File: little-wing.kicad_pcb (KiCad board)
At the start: 2 copper layers, 116.8 x 96 mm, 72 parts, among them IC1 AP7335-WG-7, J1 nice!view, J2 Battery, J3 trackball, J4 trackball, SW1 Power, SW2 Reset, U1 nice!nano v2, U2 PMW3610

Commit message: Wiring up the MCU block
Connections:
- U1 pad 7: CS_T -> CS_D
- U1 pad 8: CS_D -> CS_T
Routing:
- net GND: track 590.5 -> 667.7 mm, vias 18 -> 19
- net Row 1: track 294.5 -> 367.0 mm, vias 17 -> 20
- net Col 5: track 16.6 -> 86.7 mm
- net Net-(D19-DIN): track 33.7 -> 102.1 mm, vias 1 -> 2
- net SCK: track 0.00 -> 66.0 mm, vias 0 -> 1
- net MOSI: track 0.00 -> 64.3 mm, vias 0 -> 2
- net MISO: track 0.00 -> 56.2 mm, vias 0 -> 1
- net Row 2: track 200.5 -> 248.9 mm, vias 6 -> 9
- net CS_T: track 0.00 -> 43.9 mm
- net VCC: track 596.4 -> 629.7 mm
- net CS_D: track 0.00 -> 31.8 mm
- net Row 0: track 407.2 -> 437.4 mm
- net Col 4: track 113.5 -> 141.6 mm
- net Col 3: track 139.6 -> 165.4 mm
- net RGB: track 187.5 -> 199.4 mm
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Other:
- outline, holes or cut-outs redrawn

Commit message: Finalizing the wiring
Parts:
- moved U1 7.63 mm to (102.3, 74.2), turned to -83.5 degrees
- moved SW1 7.28 mm to (97.8, 102.6), turned to -83.5 degrees
- moved D16 7.25 mm to (109.1, 141.4), turned to 18 degrees
- moved J1 7.25 mm to (98.8, 95.2), turned to 96.5 degrees
- moved D19 7.13 mm to (106.4, 134.8), turned to 108 degrees
- moved J2 7.00 mm to (100.5, 112.0), turned to 96.5 degrees
- moved SW2 6.68 mm to (104.8, 98.1), turned to -173.5 degrees
- moved S16 6.61 mm to (110.8, 133.3), turned to 108 degrees
- moved D1 6.42 mm to (118.9, 68.6), turned to -90 degrees
- moved D20 5.88 mm to (126.0, 67.8), turned to -1.80411e-15 degrees
- moved S1 5.51 mm to (126.0, 72.5), turned to -1.80411e-15 degrees
- moved J4 5.51 mm to (113.3, 104.8), turned to -83.5 degrees
- moved D4 5.27 mm to (137.8, 65.6), turned to -90 degrees
- moved D32 5.27 mm to (202.0, 81.9), turned to -1.80411e-15 degrees
- moved D2 5.23 mm to (118.8, 89.0), turned to -90 degrees
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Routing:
- net GND: track 667.7 -> 763.2 mm, vias 19 -> 23
- net Net-(D18-DIN): track 0.00 -> 59.1 mm, vias 0 -> 4
- net VCC: track 629.7 -> 681.9 mm, vias 26 -> 31
- net Row 2: track 248.9 -> 281.6 mm
- net Row 1: track 367.0 -> 391.8 mm, vias 20 -> 22
- net Net-(D19-DIN): track 102.1 -> 121.5 mm, vias 2 -> 4
- net Col 5: track 86.7 -> 96.6 mm
- net Col 0: track 228.4 -> 230.3 mm
- net Col 1: track 201.3 -> 203.0 mm
- net RESET: track 51.9 -> 53.6 mm
- net Net-(D17-A): track 27.0 -> 28.5 mm
- net Net-(D16-A): track 28.5 -> 27.3 mm
- net Row 0: track 437.4 -> 438.6 mm
- net Col 2: track 177.4 -> 178.5 mm
- net Col 3: track 165.4 -> 166.4 mm
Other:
- board size 116.8 x 96 mm -> 119.8 x 94.8 mm

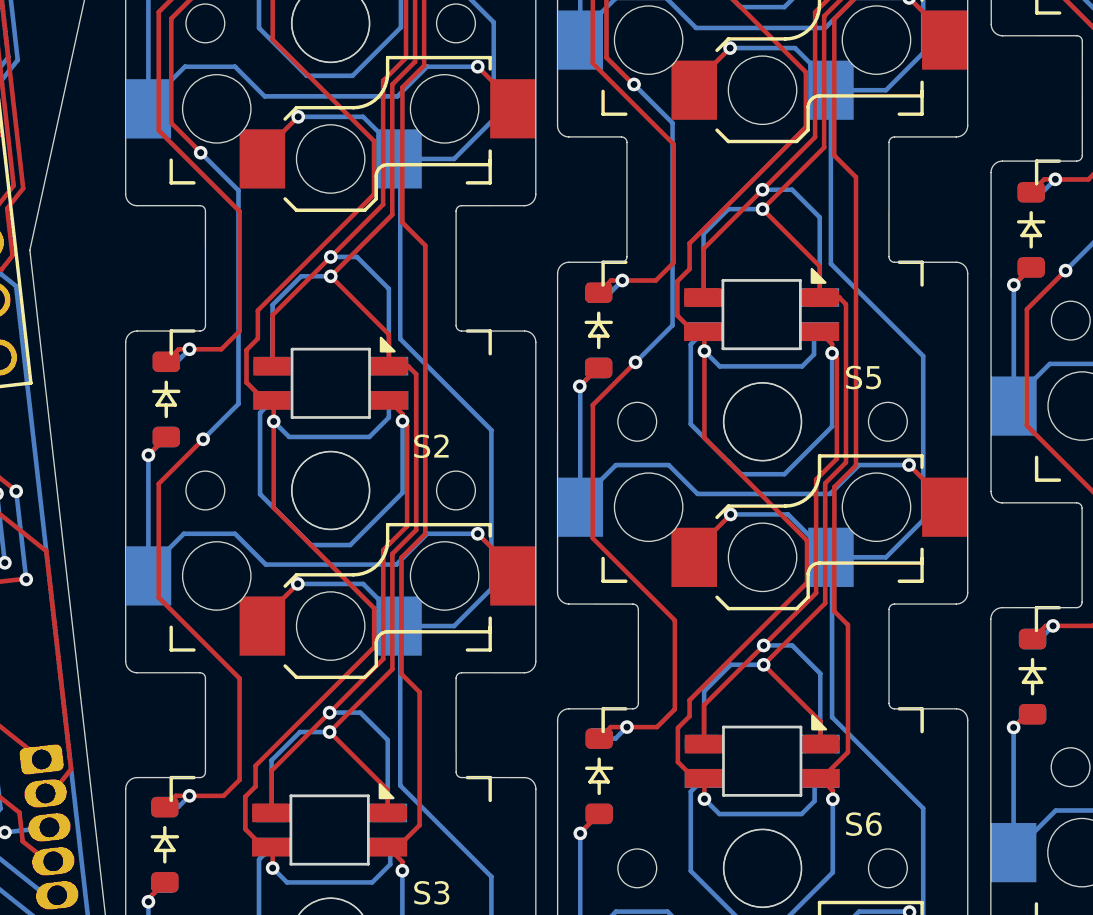
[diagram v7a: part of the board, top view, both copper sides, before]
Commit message: Repairing the cutouts and adding the flex markings
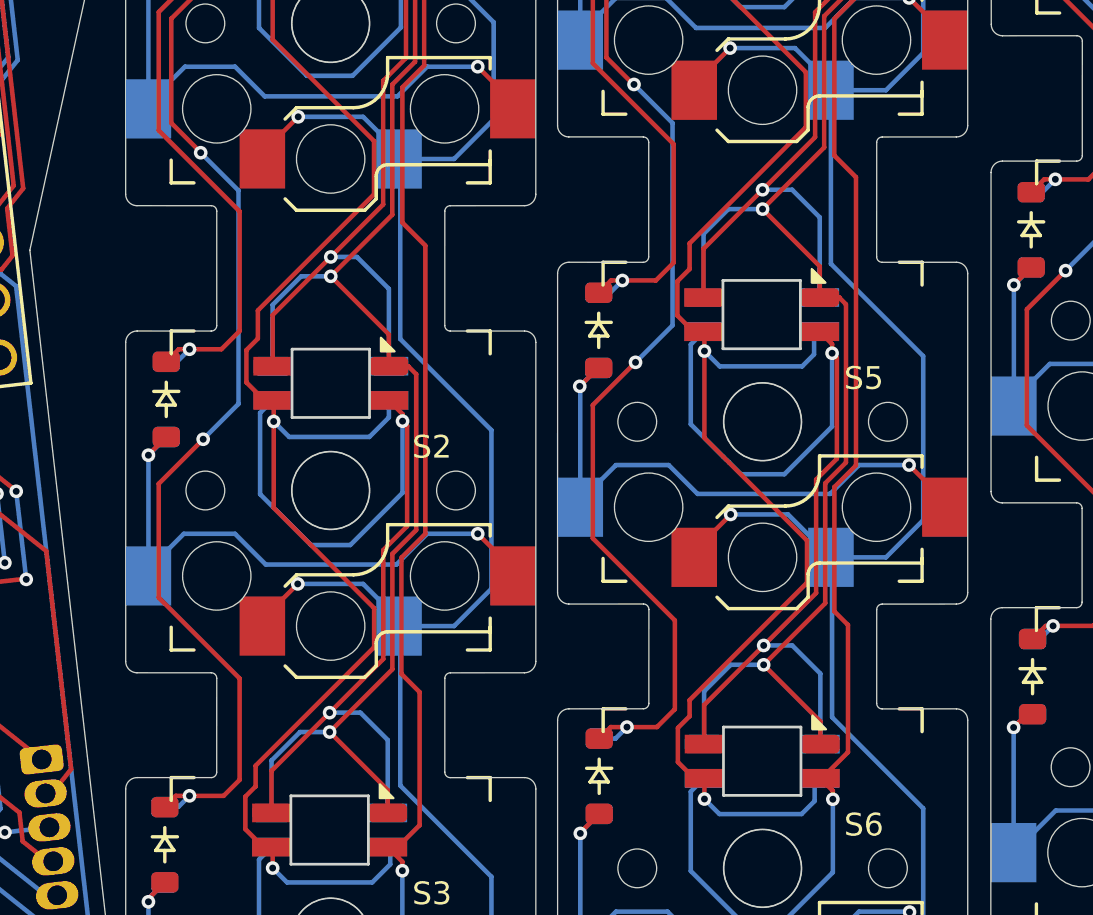
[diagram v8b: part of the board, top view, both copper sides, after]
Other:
- outline, holes or cut-outs redrawn
- board text added: "Shaded ares are flex not stiffeners are required"
